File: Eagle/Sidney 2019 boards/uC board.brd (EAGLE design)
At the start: 100 x 100 mm, 55 parts, among them J1 39-28-1043

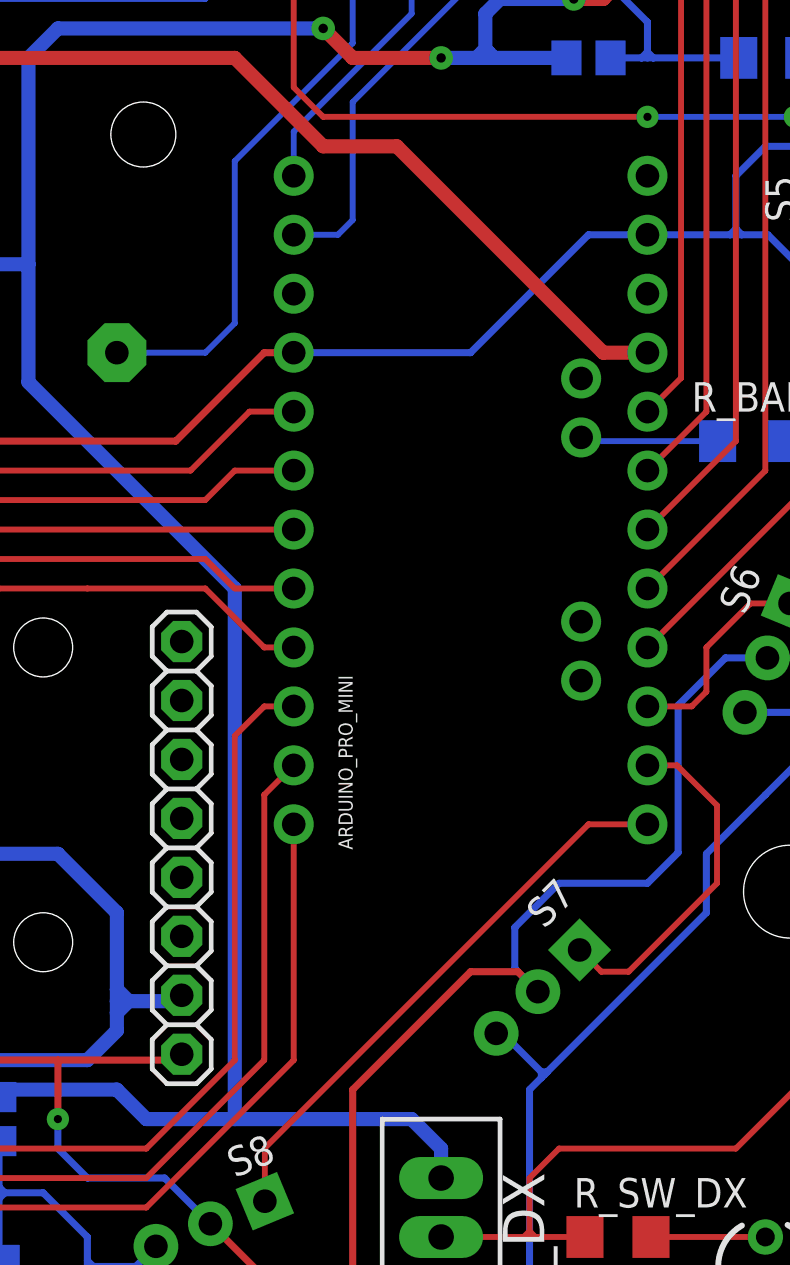
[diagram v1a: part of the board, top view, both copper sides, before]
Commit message: Added grove connectors for auxiliary supply
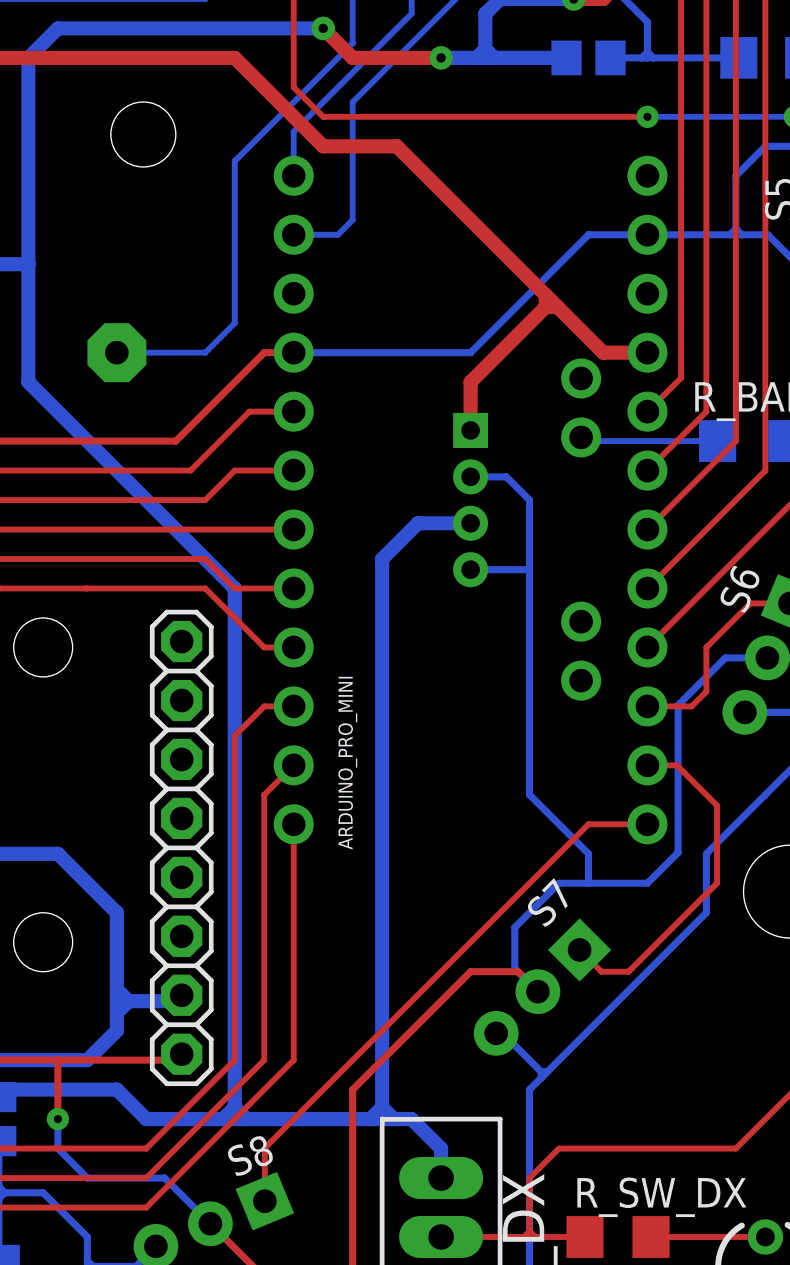
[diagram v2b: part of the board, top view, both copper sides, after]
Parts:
- added SUPPLY2_CON: TWIG_2.0, CONNECTER:2.0_1X4
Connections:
- net +5V: now also SUPPLY2_CON.1
- net +5V/S: now also SUPPLY2_CON.3
- net GND: now also SUPPLY2_CON.2, SUPPLY2_CON.4
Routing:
- net +5V/S: track 318.8 -> 350.2 mm
- net GND: track 653.8 -> 676.8 mm
- net +5V: track 219.6 -> 227.6 mm
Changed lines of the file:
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@@
 <attribute name="RS_PRICE-STOCK" value="http://uk.rs-online.com/web/p/products/4841899P" x="27.94" y="50.8" size="1.778" layer="28" rot="MR0" display="off"/>
+</element>
+<element name="SUPPLY2_CON" library="CONNECTER" package="2.0_1X4" value="TWIG_2.0" x="78.74" y="39.37" smashed="yes" rot="MR270">
+<attribute name="NAME" x="76.159" y="44.307" size="0.8128" layer="26" font="vector" ratio="10" rot="MR270"/>
+<attribute name="NAME" x="77.94" y="44.17" size="0.8128" layer="34" font="vector" ratio="10" rot="MR270"/>
 </element>
 </elements>
@@
 <wire x1="87.6808" y1="30.5308" x2="87.6808" y2="24.1808" width="0.3048" layer="16"/>
 <wire x1="80.645" y1="19.185" x2="81.64" y2="18.19" width="0.3048" layer="16"/>
-<wire x1="86.36" y1="22.86" x2="82.55" y2="22.86" width="0.3048" layer="16"/>
+<wire x1="86.36" y1="22.86" x2="83.82" y2="22.86" width="0.3048" layer="16"/>
+<wire x1="83.82" y1="22.86" x2="82.55" y2="22.86" width="0.3048" layer="16"/>
 <wire x1="82.55" y1="22.86" x2="80.645" y2="20.955" width="0.3048" layer="16"/>
 <wire x1="80.645" y1="20.955" x2="80.645" y2="19.185" width="0.3048" layer="16"/>
@@
 <wire x1="24.13" y1="50.94" x2="24.13" y2="50.8" width="0.3048" layer="1"/>
 <wire x1="30.04" y1="58.15" x2="25.84" y2="52.65" width="0.3048" layer="1"/>
+<contactref element="SUPPLY2_CON" pad="2"/>
+<contactref element="SUPPLY2_CON" pad="4"/>
+<wire x1="78.74" y1="40.37" x2="80.28" y2="40.37" width="0.3048" layer="16"/>
+<wire x1="80.28" y1="40.37" x2="81.28" y2="39.37" width="0.3048" layer="16"/>
+<wire x1="81.28" y1="39.37" x2="81.28" y2="36.322" width="0.3048" layer="16"/>
+<wire x1="81.28" y1="36.322" x2="81.28" y2="26.67" width="0.3048" layer="16"/>
+<wire x1="81.28" y1="26.67" x2="83.82" y2="24.13" width="0.3048" layer="16"/>
+<wire x1="83.82" y1="24.13" x2="83.82" y2="22.86" width="0.3048" layer="16"/>
+<wire x1="78.74" y1="36.37" x2="81.232" y2="36.37" width="0.3048" layer="16"/>
+<wire x1="81.232" y1="36.37" x2="81.28" y2="36.322" width="0.3048" layer="16"/>
 </signal>
 <signal name="SP3">
@@
 <wire x1="84.455" y1="45.72" x2="86.36" y2="45.72" width="0.6096" layer="1"/>
 <wire x1="68.58" y1="58.42" x2="72.39" y2="54.61" width="0.6096" layer="1"/>
-<wire x1="84.455" y1="45.72" x2="75.565" y2="54.61" width="0.6096" layer="1"/>
+<wire x1="84.455" y1="45.72" x2="82.4865" y2="47.6885" width="0.6096" layer="1"/>
+<wire x1="82.4865" y1="47.6885" x2="82.2325" y2="47.9425" width="0.6096" layer="1"/>
+<wire x1="82.2325" y1="47.9425" x2="81.9785" y2="48.1965" width="0.6096" layer="1"/>
+<wire x1="81.9785" y1="48.1965" x2="75.565" y2="54.61" width="0.6096" layer="1"/>
 <wire x1="75.565" y1="54.61" x2="72.39" y2="54.61" width="0.6096" layer="1"/>
 <wire x1="47.752" y1="50.8" x2="48.26" y2="51.308" width="0.6096" layer="1"/>
 <wire x1="48.26" y1="51.308" x2="48.768" y2="50.8" width="0.6096" layer="1"/>
+<contactref element="SUPPLY2_CON" pad="1"/>
+<wire x1="78.74" y1="42.37" x2="78.74" y2="44.45" width="0.6096" layer="1"/>
+<wire x1="78.74" y1="44.45" x2="81.9785" y2="47.6885" width="0.6096" layer="1"/>
+<wire x1="82.2325" y1="47.9425" x2="81.9785" y2="47.6885" width="0.6096" layer="1"/>
+<wire x1="81.9785" y1="48.1965" x2="81.9785" y2="47.6885" width="0.6096" layer="1"/>
+<wire x1="81.9785" y1="47.6885" x2="82.4865" y2="47.6885" width="0.6096" layer="1"/>
 </signal>
 <signal name="TX3">
@@
 <wire x1="79.502" y1="58.547" x2="79.502" y2="58.42" width="0.6096" layer="16"/>
 <wire x1="77.47" y1="11.43" x2="77.47" y2="10.16" width="0.6096" layer="16"/>
-<wire x1="64.77" y1="12.7" x2="68.58" y2="12.7" width="0.6096" layer="16"/>
-<wire x1="68.58" y1="12.7" x2="76.2" y2="12.7" width="0.6096" layer="16"/>
+<wire x1="64.77" y1="12.7" x2="68.072" y2="12.7" width="0.6096" layer="16"/>
+<wire x1="68.58" y1="12.7" x2="68.072" y2="12.7" width="0.6096" layer="16"/>
+<wire x1="68.58" y1="12.7" x2="69.088" y2="12.7" width="0.6096" layer="16"/>
+<wire x1="69.088" y1="12.7" x2="74.422" y2="12.7" width="0.6096" layer="16"/>
+<wire x1="74.93" y1="12.7" x2="74.422" y2="12.7" width="0.6096" layer="16"/>
+<wire x1="74.93" y1="12.7" x2="75.438" y2="12.7" width="0.6096" layer="16"/>
+<wire x1="75.438" y1="12.7" x2="76.2" y2="12.7" width="0.6096" layer="16"/>
 <wire x1="95.25" y1="64.135" x2="93.345" y2="62.23" width="0.6096" layer="16"/>
 <wire x1="85.725" y1="62.23" x2="93.345" y2="62.23" width="0.6096" layer="16"/>
@@
 <wire x1="28.575" y1="49.53" x2="54.61" y2="49.53" width="0.6096" layer="1"/>
 <wire x1="59.69" y1="44.45" x2="68.58" y2="35.56" width="0.6096" layer="16"/>
-<wire x1="68.58" y1="35.56" x2="68.58" y2="12.7" width="0.6096" layer="16"/>
+<wire x1="68.58" y1="35.56" x2="68.58" y2="13.208" width="0.6096" layer="16"/>
+<wire x1="68.58" y1="13.208" x2="68.58" y2="12.7" width="0.6096" layer="16"/>
 <wire x1="63.5" y1="13.97" x2="58.74" y2="13.97" width="0.6096" layer="16"/>
 <wire x1="58.74" y1="13.97" x2="58.42" y2="13.65" width="0.6096" layer="16"/>
+<contactref element="SUPPLY2_CON" pad="3"/>
+<wire x1="68.072" y1="12.7" x2="68.58" y2="13.208" width="0.6096" layer="16"/>
+<wire x1="68.58" y1="13.208" x2="69.088" y2="12.7" width="0.6096" layer="16"/>
+<wire x1="78.74" y1="38.37" x2="76.47" y2="38.37" width="0.6096" layer="16"/>
+<wire x1="74.93" y1="36.83" x2="74.93" y2="13.208" width="0.6096" layer="16"/>
+<wire x1="74.93" y1="13.208" x2="74.93" y2="12.7" width="0.6096" layer="16"/>
+<wire x1="76.47" y1="38.37" x2="74.93" y2="36.83" width="0.6096" layer="16"/>
+<wire x1="74.422" y1="12.7" x2="74.93" y2="13.208" width="0.6096" layer="16"/>
+<wire x1="74.93" y1="13.208" x2="75.438" y2="12.7" width="0.6096" layer="16"/>
 </signal>
 <signal name="S1_IN">
